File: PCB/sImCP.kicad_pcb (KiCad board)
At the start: 2 copper layers, 155.6 x 140 mm, 79 parts, among them J1 AVR-ISP-6, M2 MountingHole, M3 MountingHole, SW1 RESET, SW2 BOOT, U1 ATmega328P-AU, Y1 16MHz

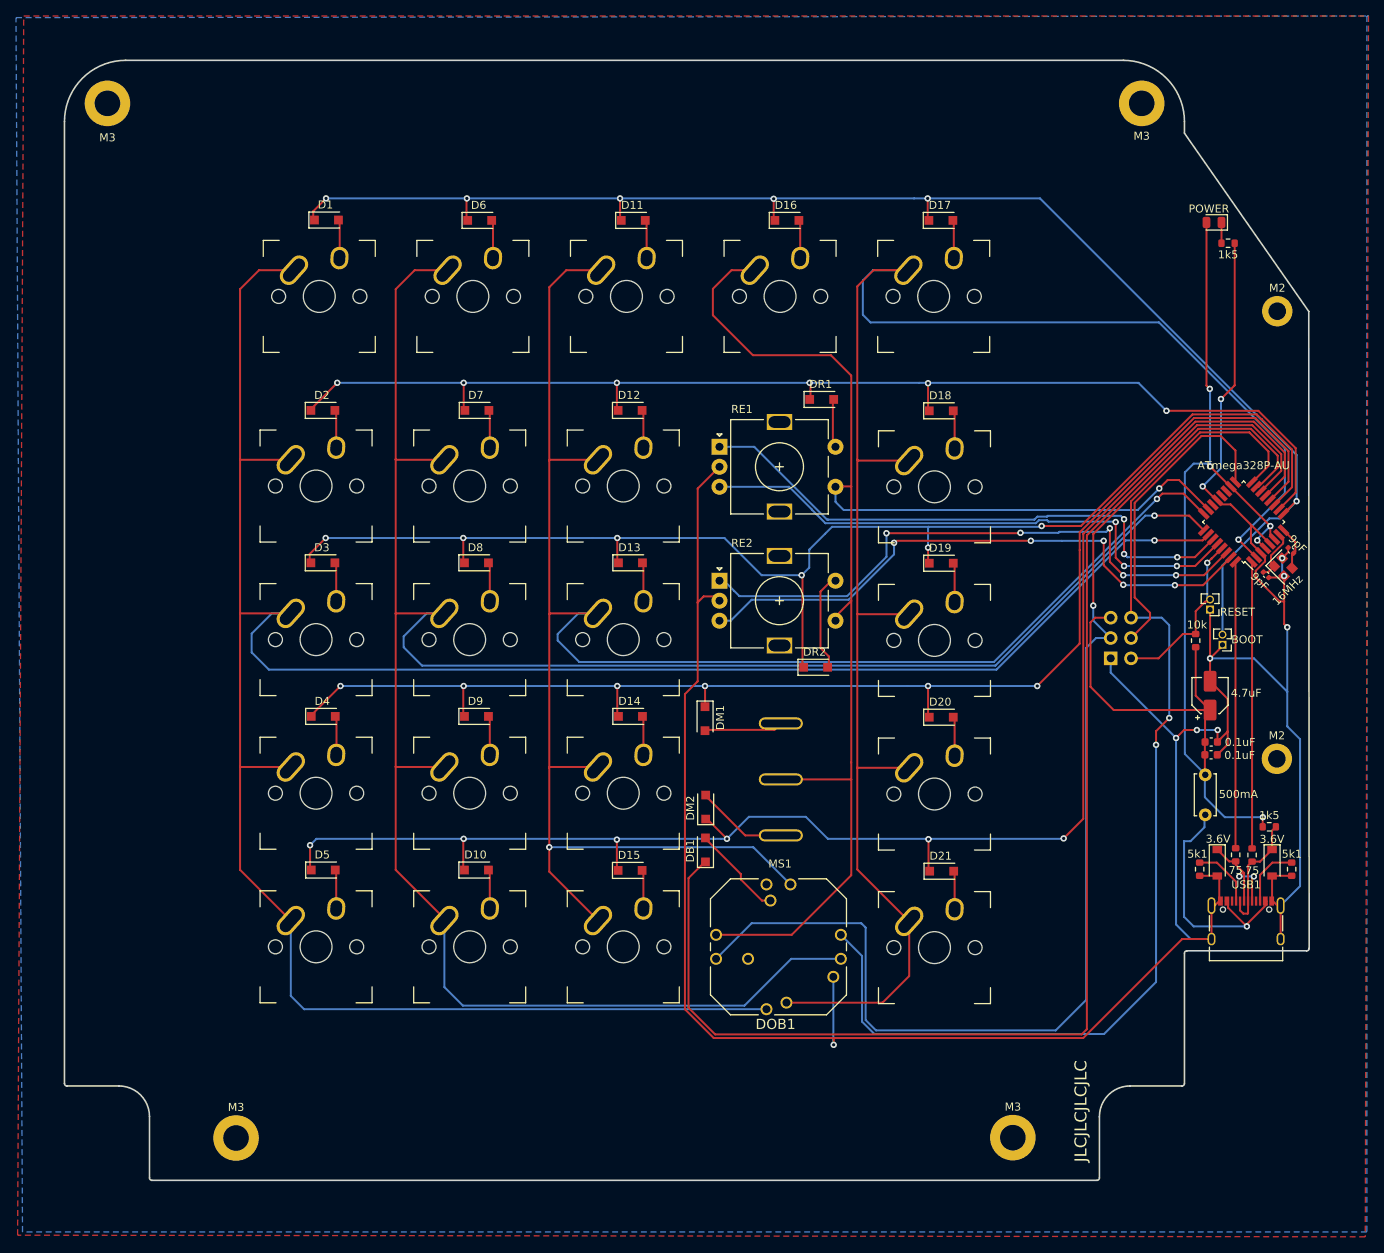
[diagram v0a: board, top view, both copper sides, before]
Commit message: rerouted with new encoder wiring
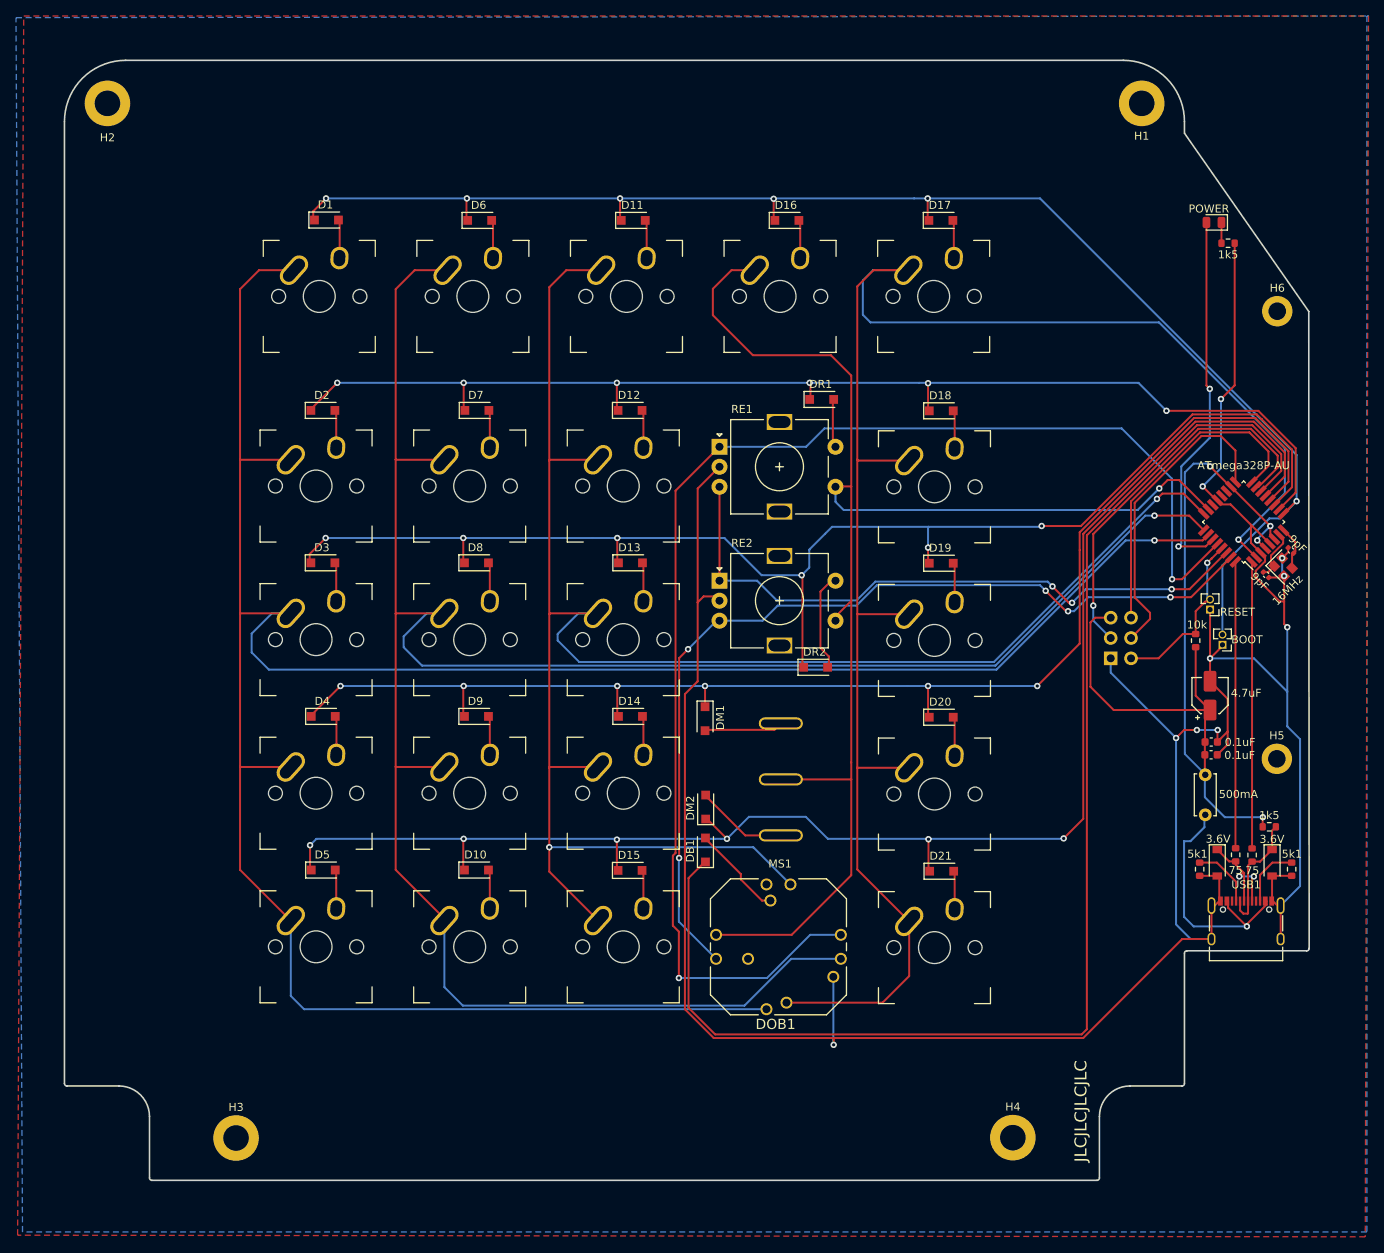
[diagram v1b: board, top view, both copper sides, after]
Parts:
- renumbered M3 to H1, M3 to H2, M3 to H3, M3 to H4, M2 to H5, M2 to H6
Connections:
- J1 pad 1: DOB1B -> MISO
- J1 pad 4: DOB1A -> MOSI
- LED1 pad 2: +5V -> POWERLED
- RE1 pad A: R1A -> DOB1B
- RE2 pad A: R2A -> R1B
- RE2 pad B: R2B -> DOB1A
- U1 pad 15: DOB1A -> MOSI
- U1 pad 16: DOB1B -> MISO
- U1 pad 27: R1A -> POWERLED
- U1 pad 28: R1B -> DOB1B
- U1 pad 30: R2A -> R1B
- U1 pad 31: R2B -> DOB1A
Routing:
- net R2A: track 75.7 -> 0.00 mm, vias 5 -> 0
- net R2B: track 74.4 -> 0.00 mm, vias 5 -> 0
- net R1A: track 71.3 -> 0.00 mm, vias 3 -> 0
- net MOSI: track 0.00 -> 48.9 mm, vias 0 -> 1
- net POWERLED: track 0.00 -> 47.0 mm, vias 0 -> 2
- net DOB1A: track 158.5 -> 116.4 mm, vias 1 -> 5
- net MISO: track 0.00 -> 41.0 mm
- net +5V: track 146.0 -> 115.3 mm, vias 5 -> 4
- net DOB1B: track 143.5 -> 171.8 mm
- net R1B: track 70.4 -> 80.8 mm
